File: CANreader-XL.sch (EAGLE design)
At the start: 73 parts, among them IC2 TJA1055T, IC3 BD9G101G, IC4 LM1117IMPX-3.3, IC5 STM32F107VBT, Q1 16MHz, U1 HC_05, U2 MCP2551, X1 MINI-USB, X2 SWD, X3 GPIO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

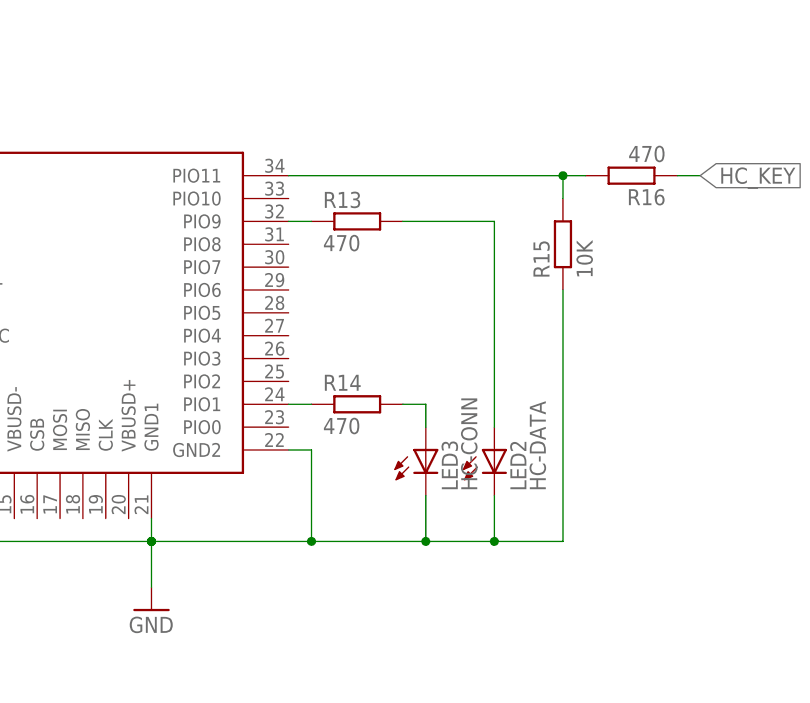
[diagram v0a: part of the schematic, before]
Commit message: HC-05 isolation, Antenna hole
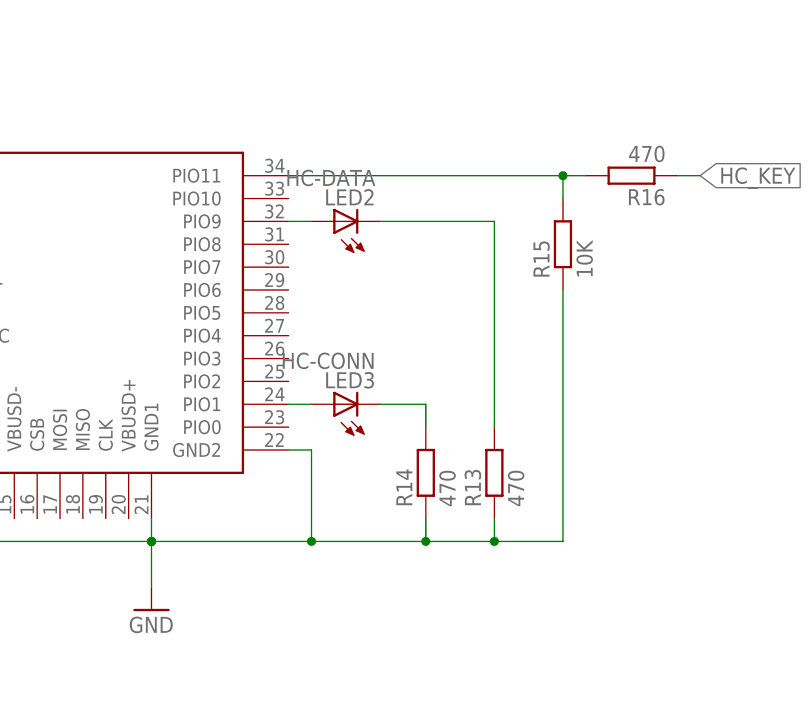
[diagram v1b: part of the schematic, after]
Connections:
- removed net N$20: R13.1, U1.PIO9
- removed net N$21: R14.1, U1.PIO1
- removed net N$22: LED2.A, R13.2
- removed net N$23: LED3.A, R14.2
- new net N$10: LED2.A, U1.PIO9
- new net N$11: LED2.C, R13.2
- new net N$13: LED3.C, R14.2
- new net N$15: LED3.A, U1.PIO1
- net GND: now also R13.1, R14.1; no longer LED2.C, LED3.C
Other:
- moved on the sheet: LED2, LED3, R13, R14
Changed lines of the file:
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@@
 <instance part="C25" gate="G$1" x="157.48" y="-93.98"/>
 <instance part="+3V5" gate="G$1" x="157.48" y="-78.74"/>
-<instance part="R13" gate="G$1" x="228.6" y="-66.04"/>
-<instance part="R14" gate="G$1" x="228.6" y="-86.36"/>
+<instance part="R13" gate="G$1" x="243.84" y="-93.98" rot="R90"/>
+<instance part="R14" gate="G$1" x="236.22" y="-93.98" rot="R90"/>
 <instance part="R15" gate="G$1" x="251.46" y="-68.58" rot="R90"/>
 <instance part="R16" gate="G$1" x="259.08" y="-60.96" rot="R180"/>
@@
 <instance part="X2" gate="A" x="-66.04" y="68.58"/>
 <instance part="X3" gate="A" x="-22.86" y="-30.48"/>
-<instance part="LED2" gate="G$1" x="243.84" y="-91.44"/>
-<instance part="LED3" gate="G$1" x="236.22" y="-91.44"/>
+<instance part="LED2" gate="G$1" x="226.06" y="-66.04" rot="R90"/>
+<instance part="LED3" gate="G$1" x="226.06" y="-86.36" rot="R90"/>
 <instance part="LED1" gate="G$1" x="124.46" y="68.58" rot="R90"/>
 <instance part="X5" gate="A" x="165.1" y="132.08"/>
@@
 <pinref part="C25" gate="G$1" pin="2"/>
 <wire x1="157.48" y1="-99.06" x2="157.48" y2="-101.6" width="0.1524" layer="91"/>
-<wire x1="243.84" y1="-96.52" x2="243.84" y2="-101.6" width="0.1524" layer="91"/>
-<wire x1="243.84" y1="-101.6" x2="236.22" y2="-101.6" width="0.1524" layer="91"/>
 <junction x="223.52" y="-101.6"/>
 <pinref part="R15" gate="G$1" pin="1"/>
+<wire x1="243.84" y1="-101.6" x2="236.22" y2="-101.6" width="0.1524" layer="91"/>
 <wire x1="236.22" y1="-101.6" x2="223.52" y2="-101.6" width="0.1524" layer="91"/>
 <wire x1="251.46" y1="-73.66" x2="251.46" y2="-101.6" width="0.1524" layer="91"/>
 <wire x1="251.46" y1="-101.6" x2="243.84" y2="-101.6" width="0.1524" layer="91"/>
+<pinref part="R13" gate="G$1" pin="1"/>
+<wire x1="243.84" y1="-99.06" x2="243.84" y2="-101.6" width="0.1524" layer="91"/>
 <junction x="243.84" y="-101.6"/>
-<wire x1="236.22" y1="-96.52" x2="236.22" y2="-101.6" width="0.1524" layer="91"/>
+<pinref part="R14" gate="G$1" pin="1"/>
+<wire x1="236.22" y1="-99.06" x2="236.22" y2="-101.6" width="0.1524" layer="91"/>
 <junction x="236.22" y="-101.6"/>
-<pinref part="LED2" gate="G$1" pin="C"/>
-<pinref part="LED3" gate="G$1" pin="C"/>
 </segment>
 <segment>
@@
 </segment>
 </net>
-<net name="N$20" class="0">
-<segment>
-<pinref part="U1" gate="G$1" pin="PIO9"/>
-<pinref part="R13" gate="G$1" pin="1"/>
-<wire x1="220.98" y1="-66.04" x2="223.52" y2="-66.04" width="0.1524" layer="91"/>
-</segment>
-</net>
-<net name="N$21" class="0">
-<segment>
-<pinref part="U1" gate="G$1" pin="PIO1"/>
-<pinref part="R14" gate="G$1" pin="1"/>
-<wire x1="220.98" y1="-86.36" x2="223.52" y2="-86.36" width="0.1524" layer="91"/>
-</segment>
-</net>
 <net name="N$25" class="0">
 <segment>
@@
 <pinref part="U1" gate="G$1" pin="RST"/>
 <wire x1="170.18" y1="-86.36" x2="172.72" y2="-86.36" width="0.1524" layer="91"/>
-</segment>
-</net>
-<net name="N$23" class="0">
-<segment>
-<pinref part="R14" gate="G$1" pin="2"/>
-<wire x1="233.68" y1="-86.36" x2="236.22" y2="-86.36" width="0.1524" layer="91"/>
-<wire x1="236.22" y1="-86.36" x2="236.22" y2="-88.9" width="0.1524" layer="91"/>
-<pinref part="LED3" gate="G$1" pin="A"/>
-</segment>
-</net>
-<net name="N$22" class="0">
-<segment>
-<pinref part="R13" gate="G$1" pin="2"/>
-<wire x1="233.68" y1="-66.04" x2="243.84" y2="-66.04" width="0.1524" layer="91"/>
-<wire x1="243.84" y1="-66.04" x2="243.84" y2="-88.9" width="0.1524" layer="91"/>
-<pinref part="LED2" gate="G$1" pin="A"/>
 </segment>
 </net>
@@
 </segment>
 </net>
+<net name="N$10" class="0">
+<segment>
+<pinref part="U1" gate="G$1" pin="PIO9"/>
+<pinref part="LED2" gate="G$1" pin="A"/>
+<wire x1="220.98" y1="-66.04" x2="223.52" y2="-66.04" width="0.1524" layer="91"/>
+</segment>
+</net>
+<net name="N$11" class="0">
+<segment>
+<pinref part="LED2" gate="G$1" pin="C"/>
+<pinref part="R13" gate="G$1" pin="2"/>
+<wire x1="231.14" y1="-66.04" x2="243.84" y2="-66.04" width="0.1524" layer="91"/>
+<wire x1="243.84" y1="-66.04" x2="243.84" y2="-88.9" width="0.1524" layer="91"/>
+</segment>
+</net>
+<net name="N$15" class="0">
+<segment>
+<pinref part="LED3" gate="G$1" pin="A"/>
+<pinref part="U1" gate="G$1" pin="PIO1"/>
+<wire x1="223.52" y1="-86.36" x2="220.98" y2="-86.36" width="0.1524" layer="91"/>
+</segment>
+</net>
+<net name="N$13" class="0">
+<segment>
+<pinref part="LED3" gate="G$1" pin="C"/>
+<pinref part="R14" gate="G$1" pin="2"/>
+<wire x1="231.14" y1="-86.36" x2="236.22" y2="-86.36" width="0.1524" layer="91"/>
+<wire x1="236.22" y1="-86.36" x2="236.22" y2="-88.9" width="0.1524" layer="91"/>
+</segment>
+</net>

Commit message: Silk layers
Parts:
- LED1: value USER -> SYS
- LED2: value HC-DATA -> BT-DAT
- LED3: value HC-CONN -> BT-CON
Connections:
- net BAT: now also C14.+, IC3.VCC
- net BAT1: no longer C14.+, IC3.VCC
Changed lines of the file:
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@@
 <part name="X2" library="pinhead" deviceset="PINHD-1X4" device="" value="SWD"/>
 <part name="X3" library="pinhead" deviceset="PINHD-2X3" device="/90" value="GPIO"/>
-<part name="LED2" library="led" deviceset="LED" device="3MM" value="HC-DATA"/>
-<part name="LED3" library="led" deviceset="LED" device="3MM" value="HC-CONN"/>
-<part name="LED1" library="led" deviceset="LED" device="3MM" value="USER"/>
+<part name="LED2" library="led" deviceset="LED" device="3MM" value="BT-DAT"/>
+<part name="LED3" library="led" deviceset="LED" device="3MM" value="BT-CON"/>
+<part name="LED1" library="led" deviceset="LED" device="3MM" value="SYS"/>
 <part name="X5" library="pinhead" deviceset="PINHD-2X3" device="/90" value="CAN"/>
 <part name="X8" library="STM32_CAN-USB" deviceset="SS12F27" device="" value="TERM"/>
@@
 <pinref part="D2" gate="G$1" pin="A"/>
 </segment>
-<segment>
-<wire x1="-5.08" y1="111.76" x2="-5.08" y2="114.3" width="0.1524" layer="91"/>
-<pinref part="C14" gate="G$1" pin="+"/>
-<pinref part="IC3" gate="G$1" pin="VCC"/>
-<wire x1="-22.86" y1="134.62" x2="-15.24" y2="134.62" width="0.1524" layer="91"/>
-<wire x1="-15.24" y1="134.62" x2="-15.24" y2="114.3" width="0.1524" layer="91"/>
-<wire x1="-15.24" y1="114.3" x2="-5.08" y2="114.3" width="0.1524" layer="91"/>
-<wire x1="-5.08" y1="114.3" x2="15.24" y2="114.3" width="0.1524" layer="91"/>
-<junction x="-5.08" y="114.3"/>
-<label x="15.24" y="114.3" size="1.778" layer="95" xref="yes"/>
-</segment>
 </net>
 <net name="N$9" class="0">
@@
 <label x="246.38" y="99.06" size="1.778" layer="95" rot="R90" xref="yes"/>
 </segment>
-</net>
+<segment>
+<pinref part="IC3" gate="G$1" pin="VCC"/>
+<wire x1="-22.86" y1="134.62" x2="-15.24" y2="134.62" width="0.1524" layer="91"/>
+<wire x1="-15.24" y1="134.62" x2="-15.24" y2="114.3" width="0.1524" layer="91"/>
+<wire x1="-15.24" y1="114.3" x2="-5.08" y2="114.3" width="0.1524" layer="91"/>
+<pinref part="C14" gate="G$1" pin="+"/>
+<wire x1="-5.08" y1="114.3" x2="7.62" y2="114.3" width="0.1524" layer="91"/>
+<wire x1="-5.08" y1="111.76" x2="-5.08" y2="114.3" width="0.1524" layer="91"/>
+<junction x="-5.08" y="114.3"/>
+<label x="7.62" y="114.3" size="1.778" layer="95" xref="yes"/>
+</segment>
+</net>

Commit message: VREF+, VREF-
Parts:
- removed X7: LAN, con-lsta:FE10-2W
- added R20, R24: 0, rcl:R-EU_R0805
- added SW1: SLEEP, STM32_CAN-USB:SS12F27
- X6: value SLEEP -> LAN; device STM32_CAN-USB:SS12F27 -> con-lsta:FE10-2W
- renumbered X8 to SW2
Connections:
- new net VREF+: IC5MCU.VREF+, R20.2
- new net VREF-: IC5MCU.VREF-, R24.2
- net +3V3: now also R20.1, X6.19, X6.20; no longer X7.19, X7.20
- net EN: now also SW1.2; no longer X6.2
- net GND: now also R24.1, SW1.3, X6.17, X6.18; no longer X6.3, X7.17, X7.18
- net N$37: now also X6.13; no longer X7.13
- net PA0: now also X6.2; no longer X7.2
- net PB10: now also X6.6; no longer X7.6
- net PB14: now also X6.8; no longer X7.8
- net PB15: now also X6.5; no longer X7.5
- net PD3: now also X6.3; no longer X7.3
- net PD4: now also X6.4; no longer X7.4
- net PD7: now also X6.1; no longer X7.1
- net RMII_CRS_DV: now also X6.14; no longer X7.14
- net RMII_MDC: now also X6.16; no longer X7.16
- net RMII_MDIO: now also X6.15; no longer X7.15
- net RMII_RXD0: now also X6.11; no longer X7.11
- net RMII_RXD1: now also X6.12; no longer X7.12
- net RMII_TXD0: now also X6.10; no longer X7.10
- net RMII_TXD1: now also X6.7; no longer X7.7
- net RMII_TX_EN: now also X6.9; no longer X7.9
- net TJA_INH: now also SW1.1; no longer X6.1

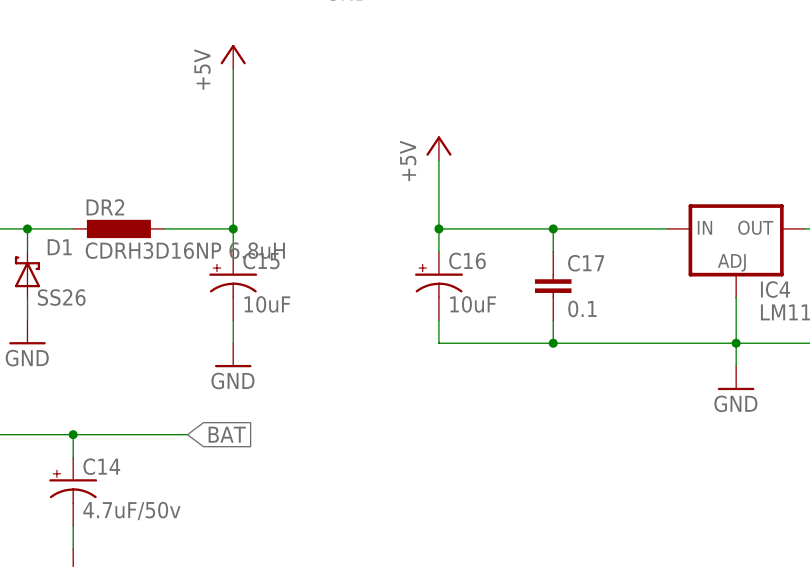
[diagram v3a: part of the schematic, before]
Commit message: Capacitors 0605 -> 0505
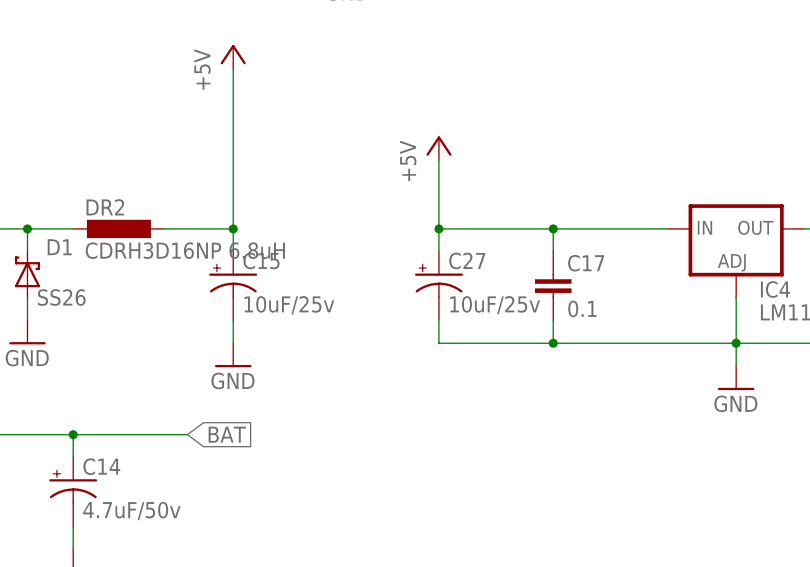
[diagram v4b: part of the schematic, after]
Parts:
- removed C16: 10uF, rcl:CPOL-US153CLV-0605
- added C27: 10uF/25v, rcl:CPOL-US153CLV-0505
- C14: device rcl:CPOL-US153CLV-0605 -> rcl:CPOL-US153CLV-0505
- C15: value 10uF -> 10uF/25v; device rcl:CPOL-US153CLV-0605 -> rcl:CPOL-US153CLV-0505
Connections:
- net +5V: now also C27.+; no longer C16.+
- net GND: now also C27.-; no longer C16.-
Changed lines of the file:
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@@
 <part name="C13" library="rcl" deviceset="C-EU" device="C0805" value="0.1"/>
 <part name="P+3" library="supply1" deviceset="+12V" device=""/>
-<part name="C14" library="rcl" deviceset="CPOL-US" device="153CLV-0605" value="4.7uF/50v"/>
 <part name="GND8" library="supply1" deviceset="GND" device=""/>
 <part name="D1" library="STM32_CAN-USB" deviceset="SCHOTTKY-DIODE" device="SMD" value="SS26"/>
 <part name="GND9" library="supply1" deviceset="GND" device=""/>
 <part name="DR2" library="STM32_CAN-USB" deviceset="CDRH3D16NP" device="" value="CDRH3D16NP 6.8uH"/>
-<part name="C15" library="rcl" deviceset="CPOL-US" device="153CLV-0605" value="10uF"/>
 <part name="GND10" library="supply1" deviceset="GND" device=""/>
 <part name="P+4" library="supply1" deviceset="+5V" device=""/>
 <part name="P+5" library="supply1" deviceset="+5V" device=""/>
 <part name="X1" library="STM32_CAN-USB" deviceset="MINI-USB-" device="UX60-MB-5ST" value="MINI-USB"/>
-<part name="C16" library="rcl" deviceset="CPOL-US" device="153CLV-0605" value="10uF"/>
 <part name="C17" library="rcl" deviceset="C-EU" device="C0805" value="0.1"/>
 <part name="C18" library="rcl" deviceset="C-EU" device="C0805" value="0.1"/>
@@
 <part name="+3V12" library="supply1" deviceset="+3V3" device=""/>
 <part name="GND25" library="supply1" deviceset="GND" device=""/>
+<part name="C15" library="rcl" deviceset="CPOL-US" device="153CLV-0505" value="10uF/25v"/>
+<part name="C14" library="rcl" deviceset="CPOL-US" device="153CLV-0505" value="4.7uF/50v"/>
+<part name="C27" library="rcl" deviceset="CPOL-US" device="153CLV-0505" value="10uF/25v"/>
 </parts>
 <sheets>
@@
 <instance part="C13" gate="G$1" x="-66.04" y="121.92"/>
 <instance part="P+3" gate="1" x="-27.94" y="190.5"/>
-<instance part="C14" gate="G$1" x="-5.08" y="109.22"/>
 <instance part="GND8" gate="1" x="-5.08" y="99.06"/>
 <instance part="D1" gate="G$1" x="-10.16" y="132.08" smashed="yes" rot="R90">
@@
 <instance part="GND9" gate="1" x="-10.16" y="124.46"/>
 <instance part="DR2" gate="G$1" x="0" y="137.16"/>
-<instance part="C15" gate="G$1" x="12.7" y="132.08"/>
 <instance part="GND10" gate="1" x="12.7" y="121.92"/>
 <instance part="P+4" gate="1" x="12.7" y="157.48"/>
 <instance part="P+5" gate="1" x="-40.64" y="106.68" rot="R270"/>
 <instance part="X1" gate="G$1" x="-25.4" y="71.12" rot="R90"/>
-<instance part="C16" gate="G$1" x="35.56" y="132.08"/>
 <instance part="C17" gate="G$1" x="48.26" y="132.08"/>
 <instance part="C18" gate="G$1" x="93.98" y="132.08"/>
@@
 </instance>
 <instance part="GND25" gate="1" x="2.54" y="25.4"/>
+<instance part="C15" gate="G$1" x="12.7" y="132.08"/>
+<instance part="C14" gate="G$1" x="-5.08" y="109.22"/>
+<instance part="C27" gate="G$1" x="35.56" y="132.08"/>
 </instances>
 <busses>
@@
 <wire x1="93.98" y1="124.46" x2="68.58" y2="124.46" width="0.1524" layer="91"/>
 <wire x1="106.68" y1="124.46" x2="106.68" y2="127" width="0.1524" layer="91"/>
-<pinref part="C16" gate="G$1" pin="-"/>
 <wire x1="35.56" y1="127" x2="35.56" y2="124.46" width="0.1524" layer="91"/>
 <wire x1="35.56" y1="124.46" x2="48.26" y2="124.46" width="0.1524" layer="91"/>
@@
 <wire x1="93.98" y1="127" x2="93.98" y2="124.46" width="0.1524" layer="91"/>
 <junction x="93.98" y="124.46"/>
+<pinref part="C27" gate="G$1" pin="-"/>
 </segment>
 <segment>
@@
 </segment>
 <segment>
-<pinref part="C14" gate="G$1" pin="-"/>
 <pinref part="GND8" gate="1" pin="GND"/>
 <wire x1="-5.08" y1="104.14" x2="-5.08" y2="101.6" width="0.1524" layer="91"/>
+<pinref part="C14" gate="G$1" pin="-"/>
 </segment>
 <segment>
@@
 </segment>
 <segment>
-<pinref part="C15" gate="G$1" pin="-"/>
 <pinref part="GND10" gate="1" pin="GND"/>
 <wire x1="12.7" y1="127" x2="12.7" y2="124.46" width="0.1524" layer="91"/>
+<pinref part="C15" gate="G$1" pin="-"/>
 </segment>
 <segment>
@@
 <wire x1="35.56" y1="144.78" x2="35.56" y2="137.16" width="0.1524" layer="91"/>
 <wire x1="35.56" y1="137.16" x2="48.26" y2="137.16" width="0.1524" layer="91"/>
-<pinref part="C16" gate="G$1" pin="+"/>
 <wire x1="48.26" y1="137.16" x2="60.96" y2="137.16" width="0.1524" layer="91"/>
 <wire x1="35.56" y1="137.16" x2="35.56" y2="134.62" width="0.1524" layer="91"/>
@@
 <wire x1="48.26" y1="134.62" x2="48.26" y2="137.16" width="0.1524" layer="91"/>
 <junction x="48.26" y="137.16"/>
+<pinref part="C27" gate="G$1" pin="+"/>
 </segment>
 <segment>
 <pinref part="DR2" gate="G$1" pin="2"/>
-<pinref part="C15" gate="G$1" pin="+"/>
 <wire x1="5.08" y1="137.16" x2="12.7" y2="137.16" width="0.1524" layer="91"/>
 <wire x1="12.7" y1="137.16" x2="12.7" y2="134.62" width="0.1524" layer="91"/>
@@
 <junction x="12.7" y="137.16"/>
 <pinref part="P+4" gate="1" pin="+5V"/>
+<pinref part="C15" gate="G$1" pin="+"/>
 </segment>
 <segment>
@@
 <wire x1="-15.24" y1="134.62" x2="-15.24" y2="114.3" width="0.1524" layer="91"/>
 <wire x1="-15.24" y1="114.3" x2="-5.08" y2="114.3" width="0.1524" layer="91"/>
-<pinref part="C14" gate="G$1" pin="+"/>
 <wire x1="-5.08" y1="114.3" x2="7.62" y2="114.3" width="0.1524" layer="91"/>
 <wire x1="-5.08" y1="111.76" x2="-5.08" y2="114.3" width="0.1524" layer="91"/>
 <junction x="-5.08" y="114.3"/>
 <label x="7.62" y="114.3" size="1.778" layer="95" xref="yes"/>
-</segment>
-</net>
+<pinref part="C14" gate="G$1" pin="+"/>
+</segment>
+</net>
